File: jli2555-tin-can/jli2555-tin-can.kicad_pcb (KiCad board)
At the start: 2 copper layers, 146.4 x 60.4 mm, 20 parts, among them J2 AudioJack3, U1 OPA134, U2 TL072

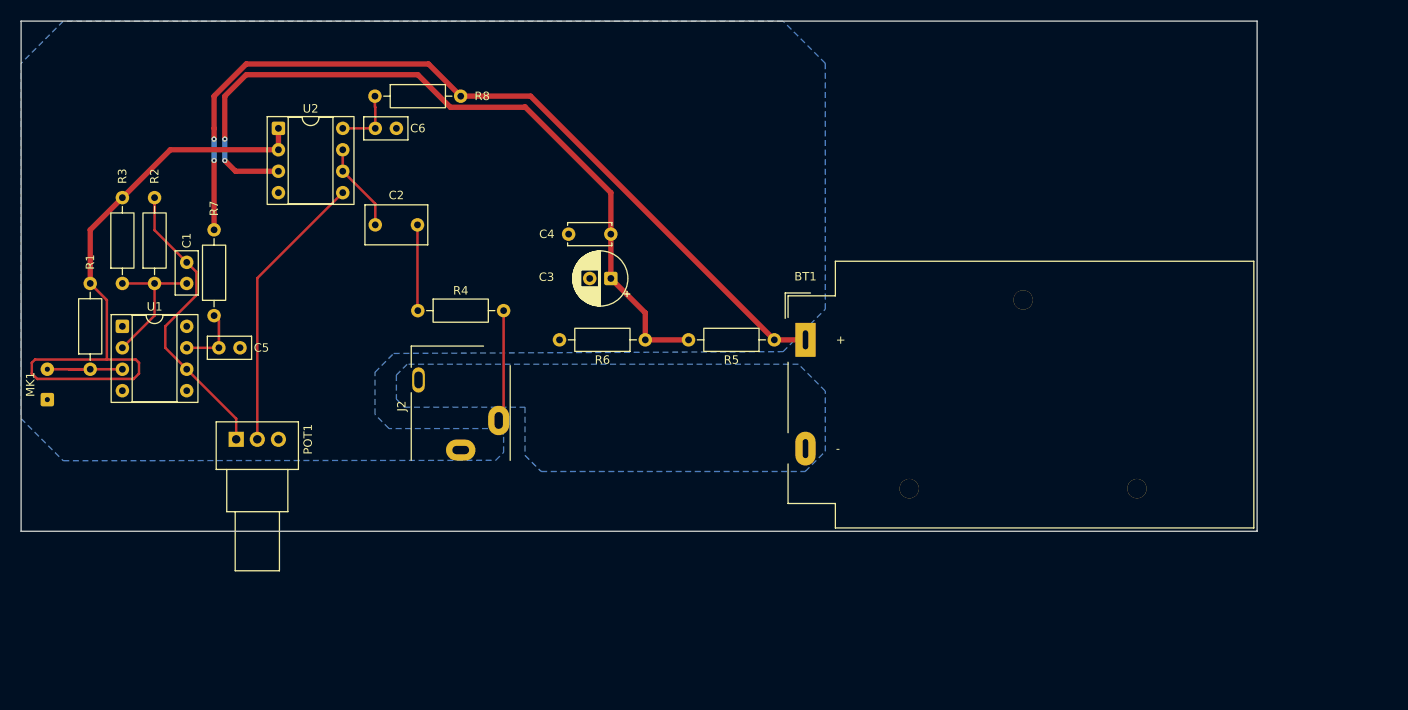
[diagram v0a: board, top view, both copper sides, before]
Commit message: finalize the -9v powered circuit design. Renamed entire project
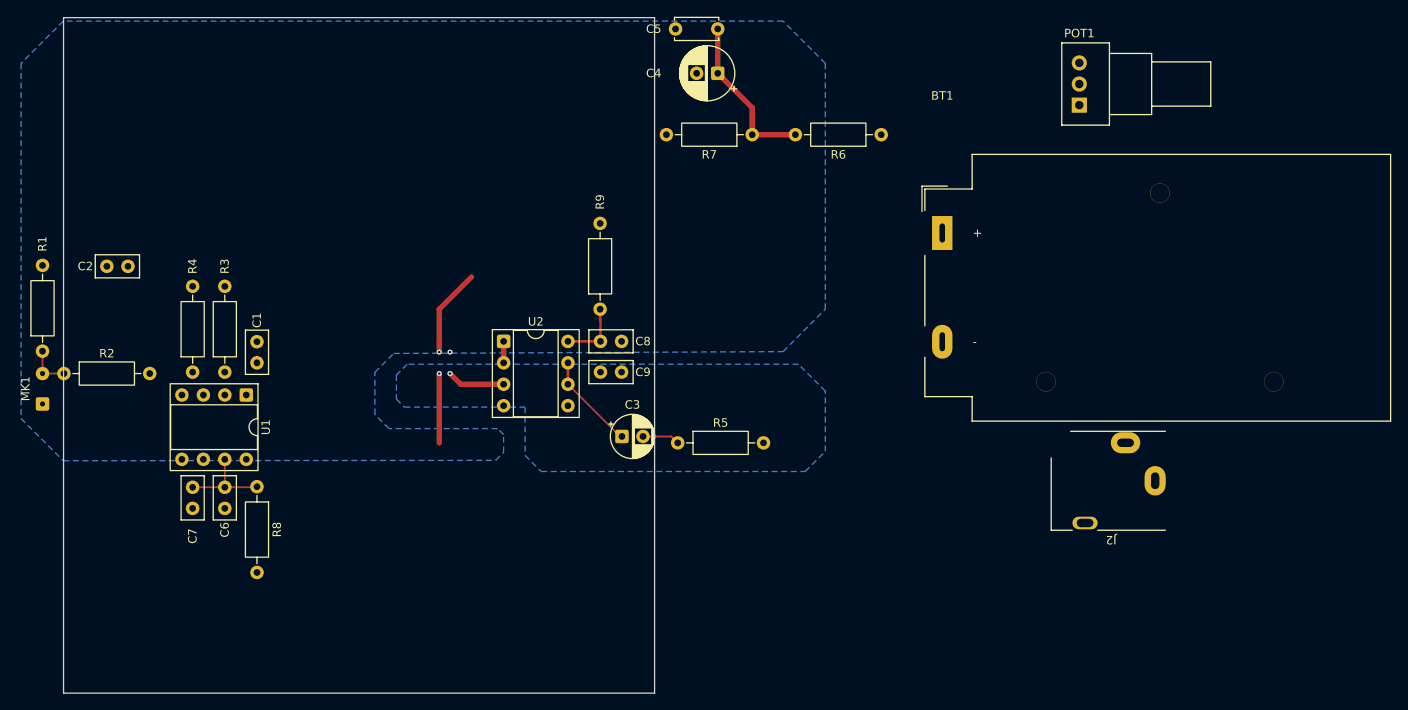
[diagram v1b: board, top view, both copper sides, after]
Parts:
- added C3: 10u, Capacitor_THT:CP_Radial_D5.0mm_P2.50mm, F.Cu at (85.1, 64.6)
- added C7: 47uF, Capacitor_THT:C_Disc_D5.0mm_W2.5mm_P2.50mm, F.Cu at (34.3, 73.1)
- added C9: 47uF, Capacitor_THT:C_Disc_D5.0mm_W2.5mm_P2.50mm, F.Cu at (85.1, 57.0)
- added R2: 1k, Resistor_THT:R_Axial_DIN0207_L6.3mm_D2.5mm_P10.16mm_Horizontal, F.Cu at (19.1, 57.1)
- C2: value 1u -> 22uF; footprint Capacitor_THT:C_Rect_L7.2mm_W4.5mm_P5.00mm_FKS2_FKP2_MKS2_MKP2 -> Capacitor_THT:C_Disc_D5.0mm_W2.5mm_P2.50mm
- R6: renamed from R5; value 10k -> 100k
- R7: renamed from R6; value 10k -> 100k
- moved POT1 107.4 mm to (139.3, 25.4), turned to 180 degrees
- moved J2 82.3 mm to (148.3, 69.8), turned to 180 degrees
- moved C8 36.7 mm to (85.1, 53.3)
- moved U2 36.7 mm to (71.1, 53.3)
- moved R9 36.7 mm to (82.5, 49.5), turned to 90 degrees
- moved R5 34.5 mm to (91.7, 65.4)
- moved C2 32.2 mm to (24.1, 44.5)
- moved C4 27.4 mm to (96.5, 21.6)
- moved C5 27.4 mm to (91.5, 16.3)
- moved R6 27.4 mm to (115.8, 28.9)
- moved R7 27.4 mm to (100.6, 28.9)
- moved R8 20.9 mm to (41.9, 70.5), turned to -90 degrees
- moved BT1 20.6 mm to (123.1, 40.5)
- moved C6 19.1 mm to (38.1, 73.1), turned to 90 degrees
- moved U1 16.8 mm to (40.6, 59.7), turned to -90 degrees
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- renumbered C3 to C4, C4 to C5, C5 to C6, C6 to C8, R2 to R3, R3 to R4, R4 to R5, R7 to R8, R8 to R9
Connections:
- C2 pad 1: Net-(U2B--) -> Vref
- POT1 pad 1: Net-(C1-Pad2) -> (no net)
- POT1 pad 2: Net-(U2B-+) -> (no net)
- POT1 pad 3: GND -> (no net)
- R4 pad 2: Vref -> Net-(C2-Pad2)
- R5 pad 1: Net-(C2-Pad2) -> Net-(C3-Pad2)
- U1 pad 3: Net-(MK1-+) -> Net-(U1A-+)
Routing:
- net +9v: track 101.0 -> 18.7 mm
- net Vref: track 73.7 -> 2.54 mm
- net Net-(U2A-+): track 91.3 -> 26.2 mm
- net Net-(C1-Pad2): track 35.8 -> 0.00 mm
- net Net-(U2B-+): track 33.4 -> 0.00 mm
- net Net-(U1A--): track 16.8 -> 0.00 mm
- net Net-(J2-PadT): track 13.3 -> 0.00 mm
- net Net-(C2-Pad2): track 10.2 -> 0.00 mm
- net Net-(MK1-+): track 11.4 -> 5.19 mm
- net Net-(C3-Pad2): track 0.00 -> 4.42 mm
- net Net-(U1B-V+): track 7.86 -> 11.0 mm
- net Net-(U2B--): track 10.5 -> 11.5 mm
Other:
- board size 146.4 x 60.4 mm -> 70 x 80 mm

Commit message: Finalization of the first printed prototype, revision 1
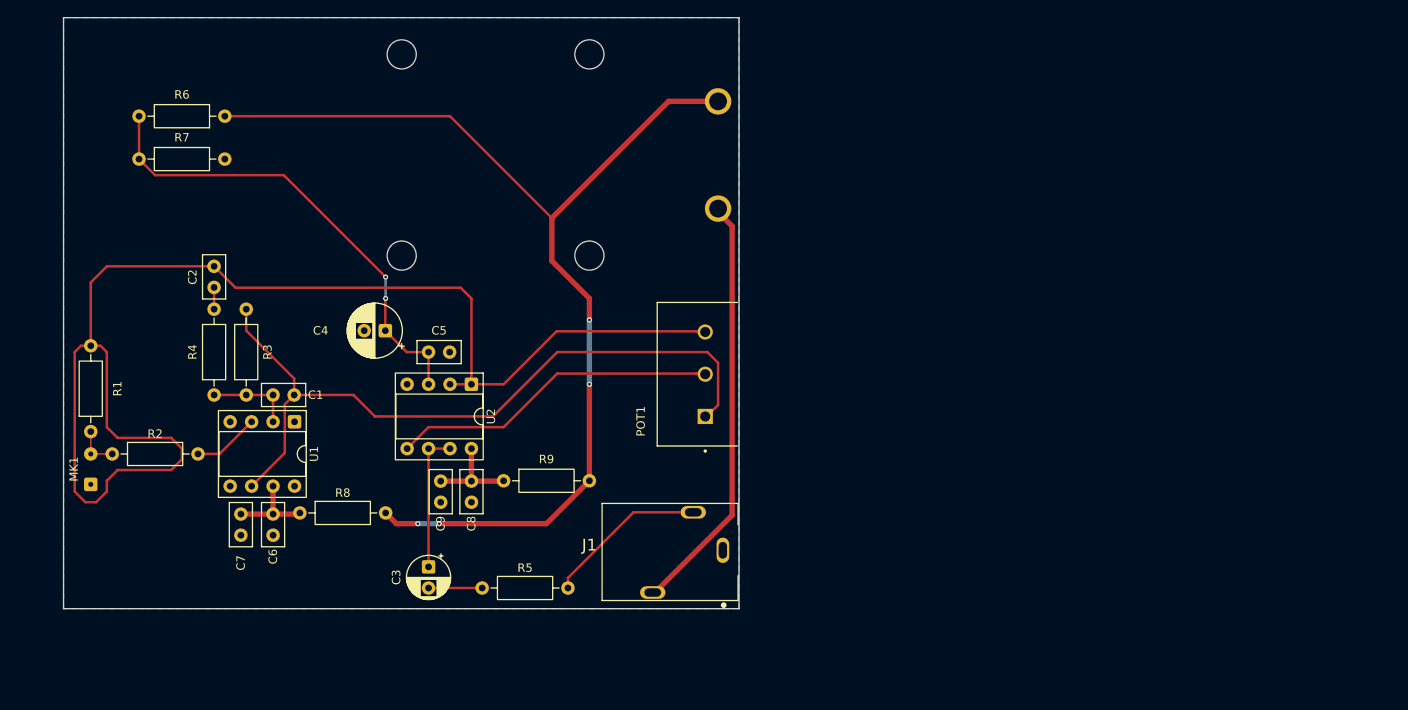
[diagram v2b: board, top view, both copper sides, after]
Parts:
- removed BT1: 9 V, Battery:BatteryHolder_MPD_BA9VPC_1xPP3
- removed J2: AudioJack3, Connector_Audio:Jack_3.5mm_CUI_SJ1-3513N_Horizontal
- added BT2: 9v, 1294:BAT_1294, B.Cu at (69.6, 31.3)
- added J1: SJ1-3513, SJ1-3513:CUI_SJ1-3513, F.Cu at (97.1, 78.1)
- C5: footprint Capacitor_THT:C_Disc_D5.0mm_W2.5mm_P5.00mm -> Capacitor_THT:C_Disc_D5.0mm_W2.5mm_P2.50mm
- POT1: footprint Potentiometer_THT:Potentiometer_Alps_RK09Y11_Single_Horizontal -> PTN16_A100120K1A1:POT_PTN16-A100120K1A1
- moved R6 77.8 mm to (38.1, 26.7)
- moved R7 72.7 mm to (27.9, 31.8), turned to 0 degrees
- moved POT1 57.6 mm to (95.0, 62.2), turned to 90 degrees
- moved C4 49.8 mm to (57.1, 52.1)
- moved C5 46.7 mm to (64.7, 54.6), turned to 180 degrees
- moved R5 28.8 mm to (68.6, 82.5)
- moved C3 27.6 mm to (62.2, 80.0), turned to -90 degrees
- moved C9 26.4 mm to (63.7, 72.4), turned to 90 degrees
- moved C8 26.1 mm to (67.3, 72.4), turned to 90 degrees
- moved R9 23.3 mm to (71.1, 69.8), turned to 0 degrees
- moved C2 12.7 mm to (36.8, 44.5), turned to -90 degrees
- moved MK1 11.1 mm to (22.2, 70.3)
- moved R1 11.1 mm to (22.2, 64.0)
- moved R2 11.1 mm to (24.8, 66.7)
- moved C7 6.54 mm to (40.0, 76.3)
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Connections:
- POT1 pad 1: (no net) -> Net-(C1-Pad2)
- POT1 pad 2: (no net) -> Net-(U2B-+)
- POT1 pad 3: (no net) -> Vref
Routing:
- net Vref: track 2.54 -> 156.4 mm
- net +9v: track 18.7 -> 128.9 mm, vias 2 -> 4
- net Net-(C1-Pad2): track 0.00 -> 87.4 mm
- net BAT -: track 0.00 -> 49.7 mm
- net Net-(U2B-+): track 0.00 -> 40.3 mm
- net Net-(U2A-+): track 26.2 -> 56.4 mm
- net Net-(J1-Pad2): track 0.00 -> 19.3 mm
- net Net-(U1A--): track 0.00 -> 10.2 mm
- net Net-(U1A-+): track 0.00 -> 7.93 mm
- net Net-(U2B--): track 11.5 -> 16.5 mm
- net Net-(U2C-V+): track 7.68 -> 11.3 mm
- net Net-(C2-Pad2): track 0.00 -> 2.58 mm
- net Net-(C3-Pad2): track 4.42 -> 6.35 mm
- net Net-(U1B-V+): track 11.0 -> 10.4 mm
- removed copper zone on B.Cu, net BAT -
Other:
- board size 70 x 80 mm -> 80 x 70 mm
